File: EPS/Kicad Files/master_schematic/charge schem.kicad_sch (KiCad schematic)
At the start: 24 parts, among them J1 USB_C_Receptacle, J2 436500212, U5 MAX77757JEFG435+, U6 MAX17055EWL+T

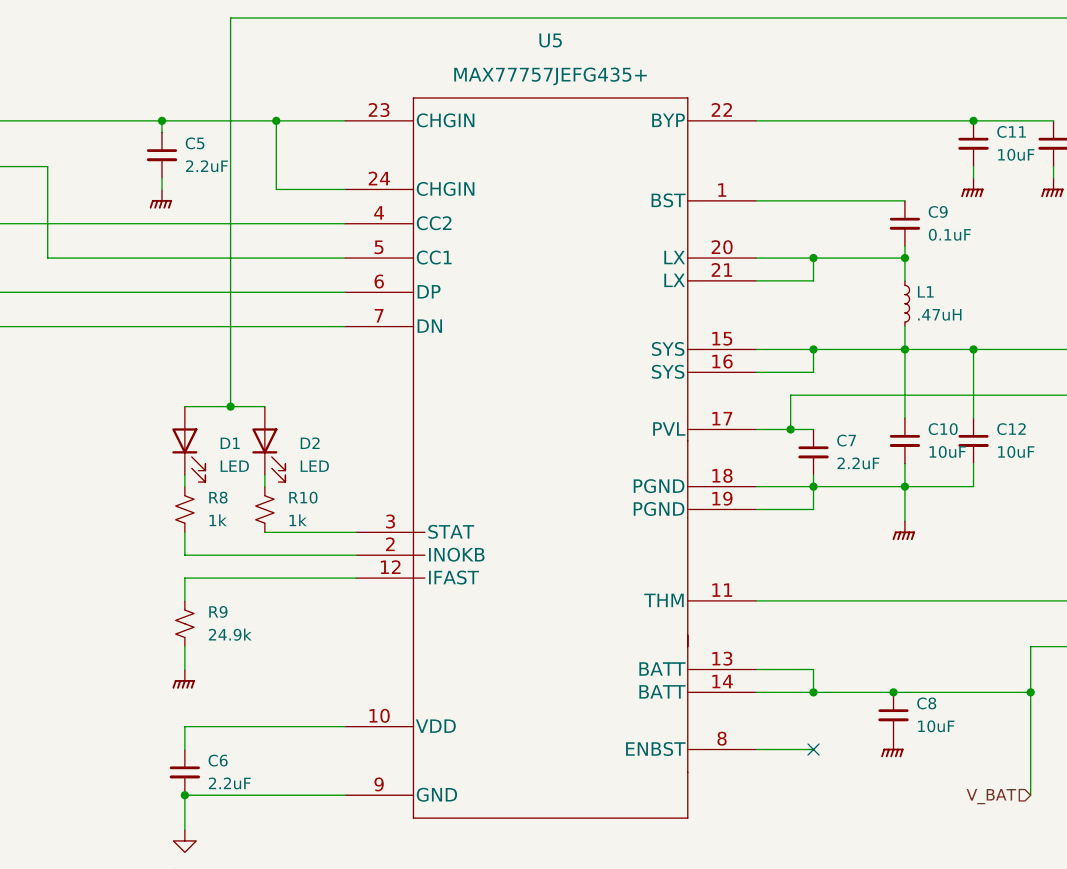
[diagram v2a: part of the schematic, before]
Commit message: EPS master netlist complete
dropped all parts onto pcb
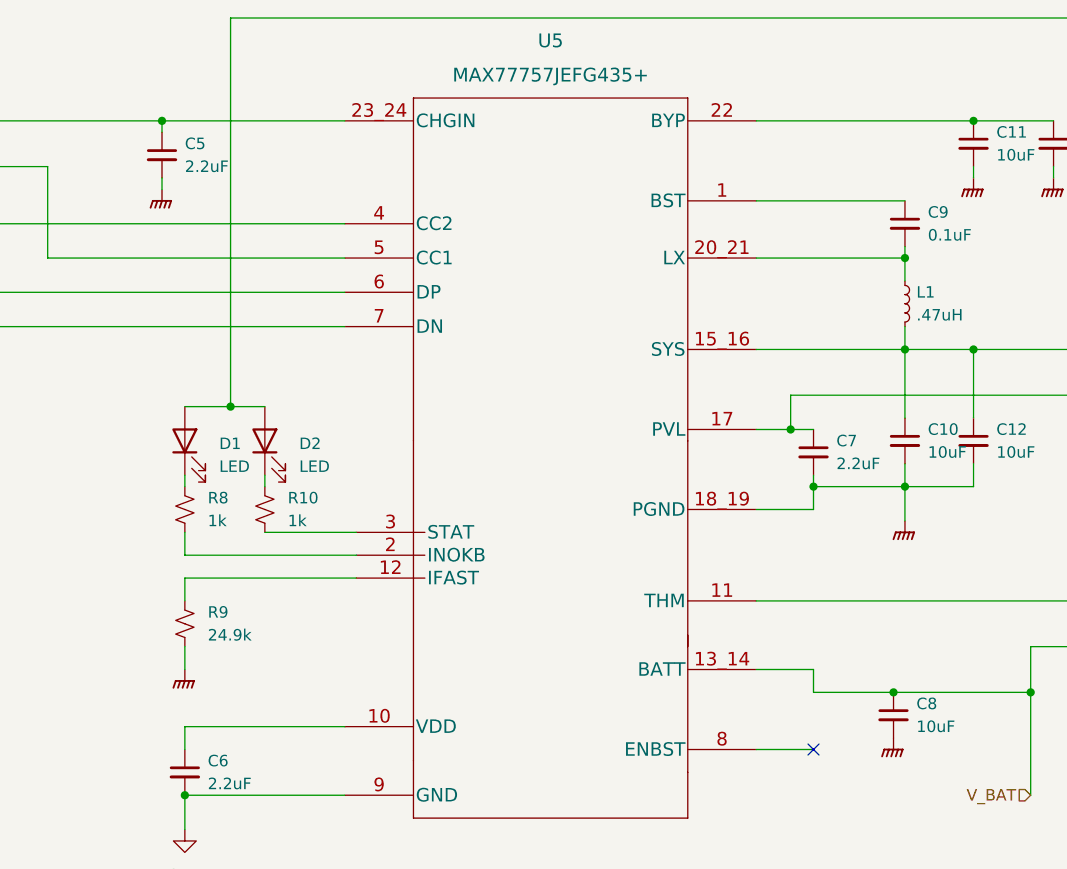
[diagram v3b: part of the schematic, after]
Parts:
- U6: footprint 17055 foot:MAX17055EWL&plus_T -> max17055:MAX17055EWL_plus_T
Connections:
- net GNDPWR: now also U5.18_19 (PGND); no longer U5.18 (PGND), U5.19 (PGND)
- net SYSPOWER: now also U5.15_16 (SYS); no longer U5.15 (SYS), U5.16 (SYS)
- net V_BAT: now also U5.13_14 (BATT); no longer U5.13 (BATT), U5.14 (BATT)
- net at C9.2, L1.1: now also U5.20_21 (LX); no longer U5.20 (LX), U5.21 (LX)
- net at C5.1, J1.A4 (VBUS), J1.A9 (VBUS)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: now also U5.23_24 (CHGIN); no longer U5.23 (CHGIN), U5.24 (CHGIN)
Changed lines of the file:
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@@
   (junction (at 218.44 93.98) (diameter 0) (color 0 0 0 0)
   )
-  (junction (at 99.06 35.56) (diameter 0) (color 0 0 0 0)
-  )
   (junction (at 200.66 88.9) (diameter 0) (color 0 0 0 0)
   )
@@
   (junction (at 168.91 76.2) (diameter 0) (color 0 0 0 0)
   )
-  (junction (at 158.75 50.8) (diameter 0) (color 0 0 0 0)
-  )
   (junction (at 176.53 60.96) (diameter 0) (color 0 0 0 0)
   )
-  (junction (at 158.75 99.06) (diameter 0) (color 0 0 0 0)
-  )
   (junction (at 168.91 60.96) (diameter 0) (color 0 0 0 0)
   )
@@
   )
   (junction (at 251.46 127) (diameter 0) (color 0 0 0 0)
-  )
-  (junction (at 158.75 60.96) (diameter 0) (color 0 0 0 0)
   )
   (no_connect (at 158.75 105.41))
@@
     (stroke (width 0) (type default) (color 0 0 0 0))
   )
-  (wire (pts (xy 158.75 50.8) (xy 168.91 50.8))
-    (stroke (width 0) (type default) (color 0 0 0 0))
-  )
   (wire (pts (xy 200.66 80.01) (xy 200.66 78.74))
     (stroke (width 0) (type default) (color 0 0 0 0))
@@
     (stroke (width 0) (type default) (color 0 0 0 0))
   )
-  (wire (pts (xy 152.4 99.06) (xy 158.75 99.06))
-    (stroke (width 0) (type default) (color 0 0 0 0))
-  )
   (wire (pts (xy 273.05 110.49) (xy 275.59 110.49))
     (stroke (width 0) (type default) (color 0 0 0 0))
@@
     (stroke (width 0) (type default) (color 0 0 0 0))
   )
-  (wire (pts (xy 152.4 60.96) (xy 158.75 60.96))
+  (wire (pts (xy 152.4 60.96) (xy 168.91 60.96))
     (stroke (width 0) (type default) (color 0 0 0 0))
   )
@@
     (stroke (width 0) (type default) (color 0 0 0 0))
   )
-  (wire (pts (xy 158.75 53.34) (xy 158.75 50.8))
-    (stroke (width 0) (type default) (color 0 0 0 0))
-  )
   (wire (pts (xy 176.53 60.96) (xy 194.31 60.96))
     (stroke (width 0) (type default) (color 0 0 0 0))
@@
     (stroke (width 0) (type default) (color 0 0 0 0))
   )
-  (wire (pts (xy 99.06 43.18) (xy 99.06 35.56))
-    (stroke (width 0) (type default) (color 0 0 0 0))
-  )
   (wire (pts (xy 176.53 68.58) (xy 176.53 60.96))
     (stroke (width 0) (type default) (color 0 0 0 0))
@@
     (stroke (width 0) (type default) (color 0 0 0 0))
   )
-  (wire (pts (xy 158.75 63.5) (xy 158.75 60.96))
-    (stroke (width 0) (type default) (color 0 0 0 0))
-  )
-  (wire (pts (xy 152.4 50.8) (xy 158.75 50.8))
+  (wire (pts (xy 152.4 50.8) (xy 168.91 50.8))
     (stroke (width 0) (type default) (color 0 0 0 0))
   )
@@
     (stroke (width 0) (type default) (color 0 0 0 0))
   )
-  (wire (pts (xy 158.75 60.96) (xy 168.91 60.96))
-    (stroke (width 0) (type default) (color 0 0 0 0))
-  )
   (wire (pts (xy 168.91 50.8) (xy 168.91 49.53))
     (stroke (width 0) (type default) (color 0 0 0 0))
@@
     (stroke (width 0) (type default) (color 0 0 0 0))
   )
-  (wire (pts (xy 106.68 43.18) (xy 99.06 43.18))
-    (stroke (width 0) (type default) (color 0 0 0 0))
-  )
   (wire (pts (xy 168.91 60.96) (xy 168.91 68.58))
     (stroke (width 0) (type default) (color 0 0 0 0))
@@
     (stroke (width 0) (type default) (color 0 0 0 0))
   )
-  (wire (pts (xy 152.4 63.5) (xy 158.75 63.5))
-    (stroke (width 0) (type default) (color 0 0 0 0))
-  )
   (wire (pts (xy 57.15 58.42) (xy 106.68 58.42))
     (stroke (width 0) (type default) (color 0 0 0 0))
   )
-  (wire (pts (xy 99.06 35.56) (xy 106.68 35.56))
+  (wire (pts (xy 86.36 35.56) (xy 106.68 35.56))
     (stroke (width 0) (type default) (color 0 0 0 0))
   )
@@
     (stroke (width 0) (type default) (color 0 0 0 0))
   )
-  (wire (pts (xy 152.4 53.34) (xy 158.75 53.34))
-    (stroke (width 0) (type default) (color 0 0 0 0))
-  )
   (wire (pts (xy 218.44 93.98) (xy 228.6 93.98))
     (stroke (width 0) (type default) (color 0 0 0 0))
   )
-  (wire (pts (xy 152.4 76.2) (xy 158.75 76.2))
-    (stroke (width 0) (type default) (color 0 0 0 0))
-  )
   (wire (pts (xy 269.24 93.98) (xy 278.13 93.98))
     (stroke (width 0) (type default) (color 0 0 0 0))
@@
   )
   (wire (pts (xy 228.6 101.6) (xy 224.79 101.6))
-    (stroke (width 0) (type default) (color 0 0 0 0))
-  )
-  (wire (pts (xy 86.36 35.56) (xy 99.06 35.56))
     (stroke (width 0) (type default) (color 0 0 0 0))
   )
@@
       (effects (font (size 1.524 1.524)))
     )
-    (property "Footprint" "17055 foot:MAX17055EWL&plus_T" (id 2) (at 248.92 86.614 0)
+    (property "Footprint" "max17055:MAX17055EWL_plus_T" (id 2) (at 248.92 86.614 0)
       (effects (font (size 1.524 1.524)) hide)
     )
@@
     (pin "11")
     (pin "12")
-    (pin "13")
-    (pin "14")
-    (pin "15")
-    (pin "16")
+    (pin "13_14")
+    (pin "15_16")
     (pin "17")
-    (pin "18")
-    (pin "19")
-    (pin "2")
-    (pin "20")
-    (pin "21")
+    (pin "18_19")
+    (pin "2")
+    (pin "20_21")
     (pin "22")
-    (pin "23")
-    (pin "24")
+    (pin "23_24")
     (pin "3")
     (pin "4")

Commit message: EPS board updated
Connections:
- net GND: now also C5.2
- net GNDPWR: no longer C5.2
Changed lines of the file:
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@@
     (effects (font (size 1.27 1.27)) (justify left))
   )
-  (symbol (lib_id "power:GNDPWR") (at 86.36 43.18 0) (unit 1)
+  (symbol (lib_id "power:GND") (at 86.36 43.18 0) (unit 1)
     (in_bom yes) (on_board yes) (fields_autoplaced)
     (property "Reference" "#PWR012" (id 0) (at 86.36 48.26 0)
@@
       (effects (font (size 1.27 1.27)) hide)
     )
-    (property "Footprint" "" (id 2) (at 86.36 44.45 0)
-      (effects (font (size 1.27 1.27)) hide)
-    )
-    (property "Datasheet" "" (id 3) (at 86.36 44.45 0)
+    (property "Footprint" "" (id 2) (at 86.36 43.18 0)
+      (effects (font (size 1.27 1.27)) hide)
+    )
+    (property "Datasheet" "" (id 3) (at 86.36 43.18 0)
       (effects (font (size 1.27 1.27)) hide)
     )
@@
     (pin "2")
   )
-  (symbol (lib_id "power:GND1") (at 218.44 99.06 0) (unit 1)
+  (symbol (lib_id "power:GND") (at 218.44 99.06 0) (unit 1)
     (in_bom yes) (on_board yes) (fields_autoplaced)
     (property "Reference" "#PWR020" (id 0) (at 218.44 105.41 0)
       (effects (font (size 1.27 1.27)) hide)
     )
-    (property "Value" "GND1" (id 1) (at 218.44 104.14 0))
+    (property "Value" "GND" (id 1) (at 218.44 104.14 0))
     (property "Footprint" "" (id 2) (at 218.44 99.06 0)
       (effects (font (size 1.27 1.27)) hide)
@@
     (pin "C3")
   )
-  (symbol (lib_id "power:GND1") (at 278.13 99.06 0) (unit 1)
+  (symbol (lib_id "power:GND") (at 278.13 99.06 0) (unit 1)
     (in_bom yes) (on_board yes) (fields_autoplaced)
     (property "Reference" "#PWR022" (id 0) (at 278.13 105.41 0)
       (effects (font (size 1.27 1.27)) hide)
     )
-    (property "Value" "GND1" (id 1) (at 278.13 104.14 0))
+    (property "Value" "GND" (id 1) (at 278.13 104.14 0))
     (property "Footprint" "" (id 2) (at 278.13 99.06 0)
       (effects (font (size 1.27 1.27)) hide)
@@
     (pin "2")
   )
-  (symbol (lib_id "power:GND1") (at 238.76 123.19 0) (unit 1)
+  (symbol (lib_id "power:GND") (at 238.76 123.19 0) (unit 1)
     (in_bom yes) (on_board yes)
     (property "Reference" "#PWR021" (id 0) (at 238.76 129.54 0)
       (effects (font (size 1.27 1.27)) hide)
     )
-    (property "Value" "GND1" (id 1) (at 236.22 120.65 0))
+    (property "Value" "GND" (id 1) (at 236.22 120.65 0))
     (property "Footprint" "" (id 2) (at 238.76 123.19 0)
       (effects (font (size 1.27 1.27)) hide)

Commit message: eps updated
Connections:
- net GND: now also R9.2
- net GNDPWR: no longer R9.2
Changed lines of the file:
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@@
     (stroke (width 0) (type default) (color 0 0 0 0))
   )
-  (wire (pts (xy 182.88 110.49) (xy 182.88 99.06))
+  (wire (pts (xy 182.88 99.06) (xy 182.88 115.57))
     (stroke (width 0) (type default) (color 0 0 0 0))
   )
@@
     (pin "2")
   )
-  (symbol (lib_id "power:GNDPWR") (at 88.9 96.52 0) (unit 1)
+  (symbol (lib_id "power:GND") (at 88.9 96.52 0) (unit 1)
     (in_bom yes) (on_board yes) (fields_autoplaced)
     (property "Reference" "#PWR013" (id 0) (at 88.9 101.6 0)
@@
       (effects (font (size 1.27 1.27)) hide)
     )
-    (property "Footprint" "" (id 2) (at 88.9 97.79 0)
-      (effects (font (size 1.27 1.27)) hide)
-    )
-    (property "Datasheet" "" (id 3) (at 88.9 97.79 0)
-      (effects (font (size 1.27 1.27)) hide)
-    )
+    (property "Footprint" "" (id 2) (at 88.9 96.52 0)
+      (effects (font (size 1.27 1.27)) hide)
+    )
+    (property "Datasheet" "" (id 3) (at 88.9 96.52 0)
+      (effects (font (size 1.27 1.27)) hide)
+    )

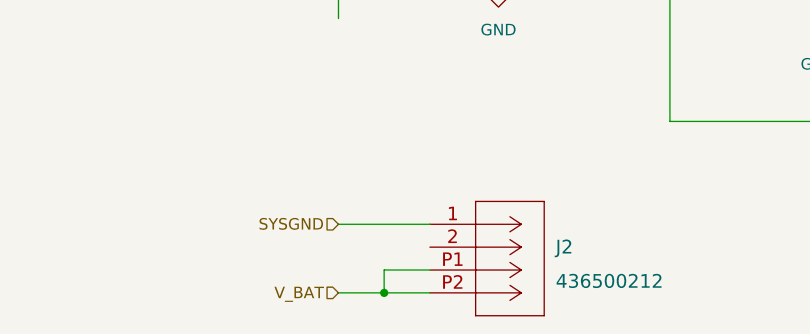
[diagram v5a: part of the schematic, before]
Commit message: all traces routed (EPS)
all nets, traces, etc connected.....now we need to run DRC...errors are inevitable
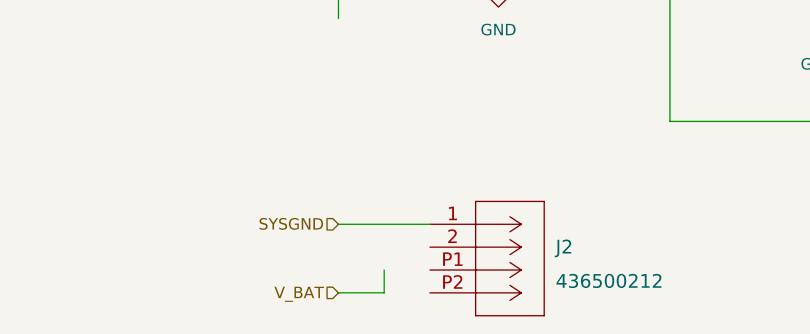
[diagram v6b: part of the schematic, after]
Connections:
- net V_BAT: no longer J2.P1, J2.P2
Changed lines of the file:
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@@
   (junction (at 200.66 78.74) (diameter 0) (color 0 0 0 0)
-  )
-  (junction (at 187.96 146.05) (diameter 0) (color 0 0 0 0)
   )
   (junction (at 168.91 50.8) (diameter 0) (color 0 0 0 0)
@@
     (stroke (width 0) (type default) (color 0 0 0 0))
   )
-  (wire (pts (xy 187.96 146.05) (xy 193.04 146.05))
-    (stroke (width 0) (type default) (color 0 0 0 0))
-  )
   (wire (pts (xy 168.91 80.01) (xy 168.91 76.2))
     (stroke (width 0) (type default) (color 0 0 0 0))
@@
     (stroke (width 0) (type default) (color 0 0 0 0))
   )
-  (wire (pts (xy 193.04 143.51) (xy 187.96 143.51))
-    (stroke (width 0) (type default) (color 0 0 0 0))
-  )

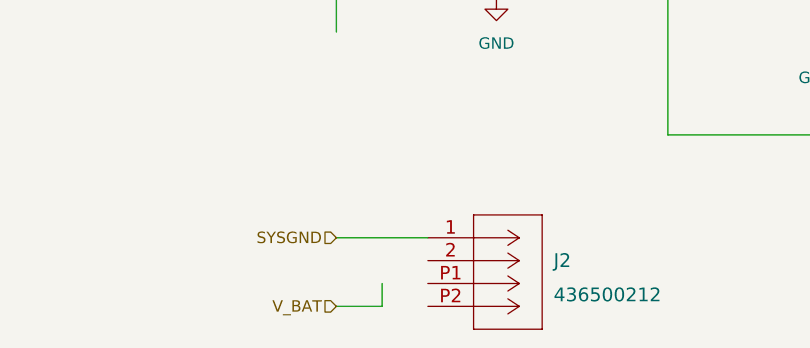
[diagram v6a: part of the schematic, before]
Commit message: [EPS] updated DRC errors
fixed/updated rules to have no errors. however the dimensions might not work with manufacturers.... also, silkscreens need to be moved/resized
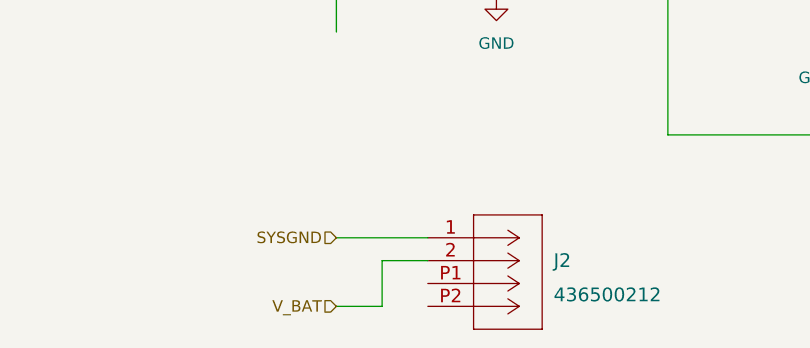
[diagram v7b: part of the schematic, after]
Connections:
- net V_BAT: now also J2.2
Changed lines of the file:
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@@
+    (stroke (width 0) (type default) (color 0 0 0 0))
+  )
+  (wire (pts (xy 193.04 140.97) (xy 187.96 140.97))
     (stroke (width 0) (type default) (color 0 0 0 0))
   )
@@
     (stroke (width 0) (type default) (color 0 0 0 0))
   )
-  (wire (pts (xy 187.96 143.51) (xy 187.96 146.05))
+  (wire (pts (xy 187.96 140.97) (xy 187.96 146.05))
     (stroke (width 0) (type default) (color 0 0 0 0))
   )

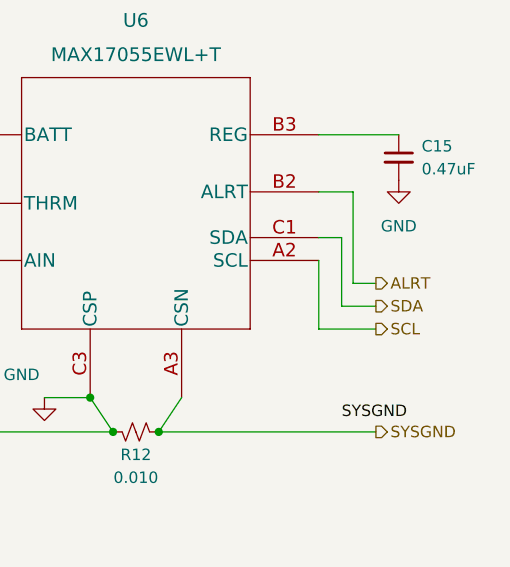
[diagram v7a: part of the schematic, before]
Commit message: Eps board update
vias fixed for manufacturers standards, eliminated ALRT pin on battery gauge
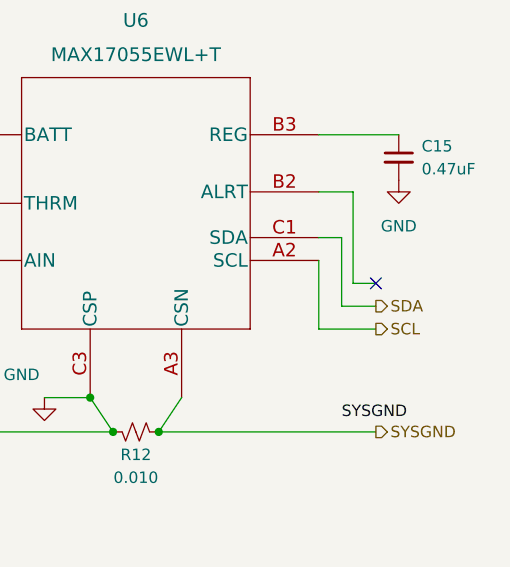
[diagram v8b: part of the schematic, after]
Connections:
- net ALRT: no longer names the net of U6.B2 (ALRT)
- no-connect marks 13 -> 14
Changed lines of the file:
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@@
   (no_connect (at 45.72 78.74))
   (no_connect (at 45.72 83.82))
+  (no_connect (at 275.59 110.49))
   (wire (pts (xy 182.88 93.98) (xy 182.88 99.06))
     (stroke (width 0) (type default) (color 0 0 0 0))
@@
     (effects (font (size 1.27 1.27)) (justify left))
   )
-  (hierarchical_label "ALRT" (shape output) (at 275.59 110.49 0)
-    (effects (font (size 1.27 1.27)) (justify left))
-  )
